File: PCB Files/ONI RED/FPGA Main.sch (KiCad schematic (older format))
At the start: 1 part

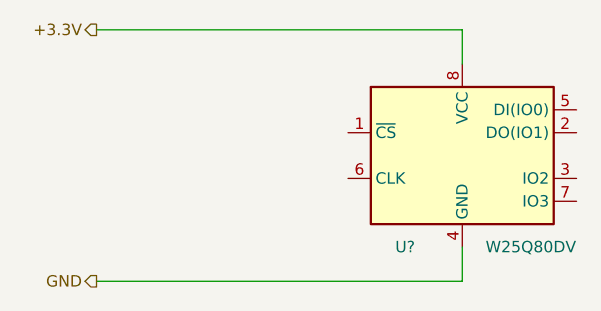
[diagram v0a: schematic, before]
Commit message: Added second ethernet PHY and started to add PCIE connections
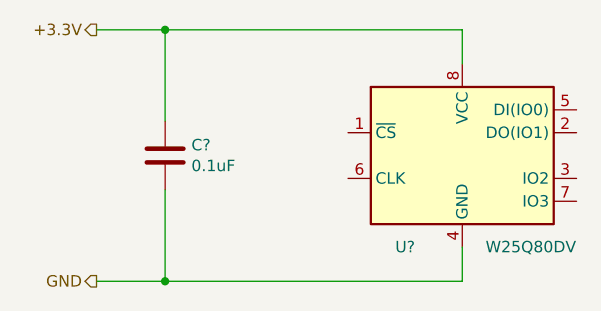
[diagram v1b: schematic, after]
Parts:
- added C?: 0.1uF, symbol Device:C
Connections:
- net +3.3V: now also C?.1
- net GND: now also C?.2
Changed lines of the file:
@@
 $Descr A4 11693 8268
 encoding utf-8
-Sheet 4 4
+Sheet 4 5
 Title ""
 Date ""
@@
 	2950 2250 2950 2100
 Wire Wire Line
-	1350 1150 2950 1150
+	1350 1150 1650 1150
 Wire Wire Line
-	1350 2250 2950 2250
+	1350 2250 1650 2250
+$Comp
+L Device:C C?
+U 1 1 5EA7C2F2
+P 1650 1700
+F 0 "C?" H 1765 1746 50  0000 L CNN
+F 1 "0.1uF" H 1765 1655 50  0000 L CNN
+F 2 "" H 1688 1550 50  0001 C CNN
+F 3 "~" H 1650 1700 50  0001 C CNN
+	1    1650 1700
+	1    0    0    -1
+$EndComp
+Wire Wire Line
+	1650 1550 1650 1150
+Connection ~ 1650 1150
+Wire Wire Line
+	1650 1150 2950 1150
+Wire Wire Line
+	1650 1850 1650 2250
+Connection ~ 1650 2250
+Wire Wire Line
+	1650 2250 2950 2250
 $EndSCHEMATC

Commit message: Continued routing work
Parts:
- added R1: 4.7k, symbol Device:R_Small
- added R2, R3, R4, R5: 10k, symbol Device:R_Small
- added U1: LFE5UM-25F-6BG381C, symbol Custom_Symbols:LFE5UM-25F-6BG381C
- gave numbers to parts that had none: 2
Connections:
- net labels added: CLKN, CLKP, RXN0, RXN1, RXP0, RXP1, TCK, TDI, TDO, TMS, TXN0, TXN1, TXP0, TXP1
- wire segments 8 -> 65
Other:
- moved on the sheet: C7, U3
